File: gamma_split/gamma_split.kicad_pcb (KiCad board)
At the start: 2 copper layers, 109 x 71 mm, 156 parts, among them J1 USB_C_Receptacle, J2 USB_C_Receptacle, J3 TC2030-IDC, J4 D4, J5 D5, J6 A6, J7 A7, J8 B0, K00 K00, K01 K01, K02 K02, K03 K03, K04 K04, K05 K05, K10 K10, K11 K11, K12 K12, K13 K13, K14 K14, K15 K15, K20 K20, K21 K21, K22 K22, K23 K23, K24 K24, K25 K25, K30 K30, K31 K31, K32 K32, K33 K33, K34 K34, K35 K35, SW1 Switch-6P-2S2T, SW2 SW_Push, U1 MCP73831, U2 MCP1700 (3.0V), U3 MCP1700 (3.3V), U4 ATXMEGA-A4U-EPAD, U5 74LVC1G34, U6 nRF24L01_module, U7 FSUSB42, U8 FSUSB42, U9 FSUSB42

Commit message: rename alpha split to gamma split
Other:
- board text added: "γ-split"
- board text removed: "α-split"
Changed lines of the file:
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@@
       (net 10 /RST))
   )
-  (gr_text α-split (at 26 35.5) (layer F.SilkS)
+  (gr_text γ-split (at 26.5 35.5) (layer F.SilkS)
     (effects (font (size 1.5 1.5) (thickness 0.3)))
   )

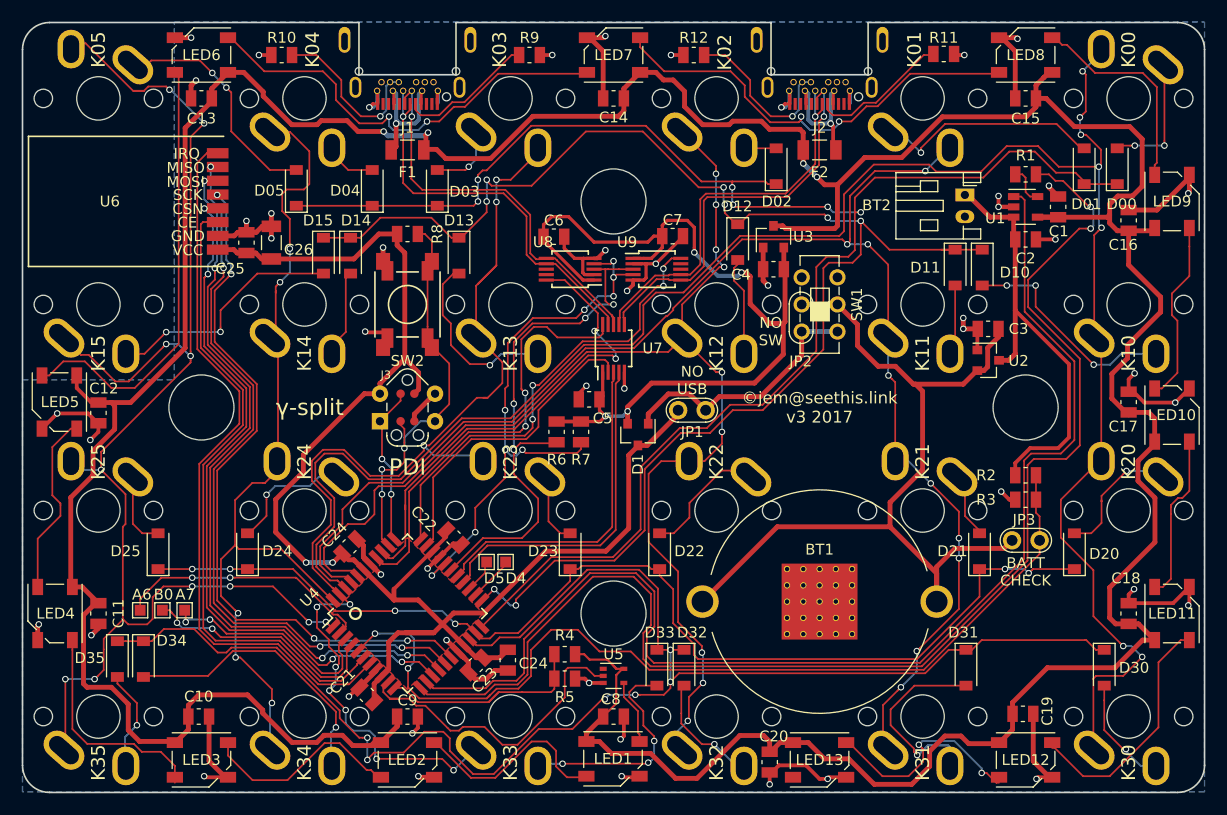
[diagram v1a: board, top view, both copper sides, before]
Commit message: remove soldermask around cr2032 battery contact
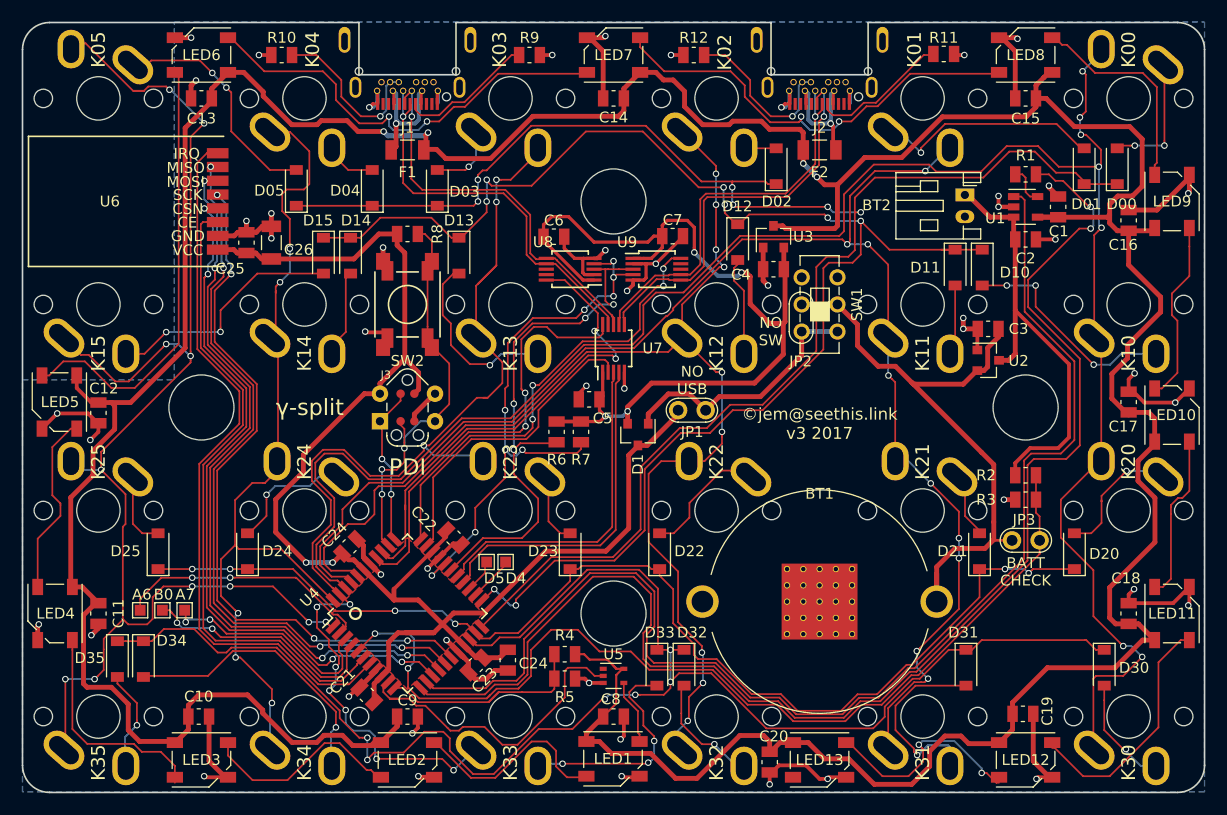
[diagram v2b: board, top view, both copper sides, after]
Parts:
- BT1: footprint battery:CR2032_BK-913 -> battery:CR2032_MPD_BK-913_NoSolderMask
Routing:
- net /BATT_IN: track 83.2 -> 59.9 mm
- net /ROW3: track 140.4 -> 145.2 mm
- net /ROW2: track 102.2 -> 106.2 mm
- net /BAT_LVL: track 87.7 -> 91.6 mm
- net /BAT_PROG: track 122.4 -> 126.3 mm
- net /BAT_STAT: track 113.1 -> 117.0 mm
- net /COL1: track 139.3 -> 141.3 mm
- net GND: track 184.7 -> 184.2 mm

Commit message: add some alternative xmegas
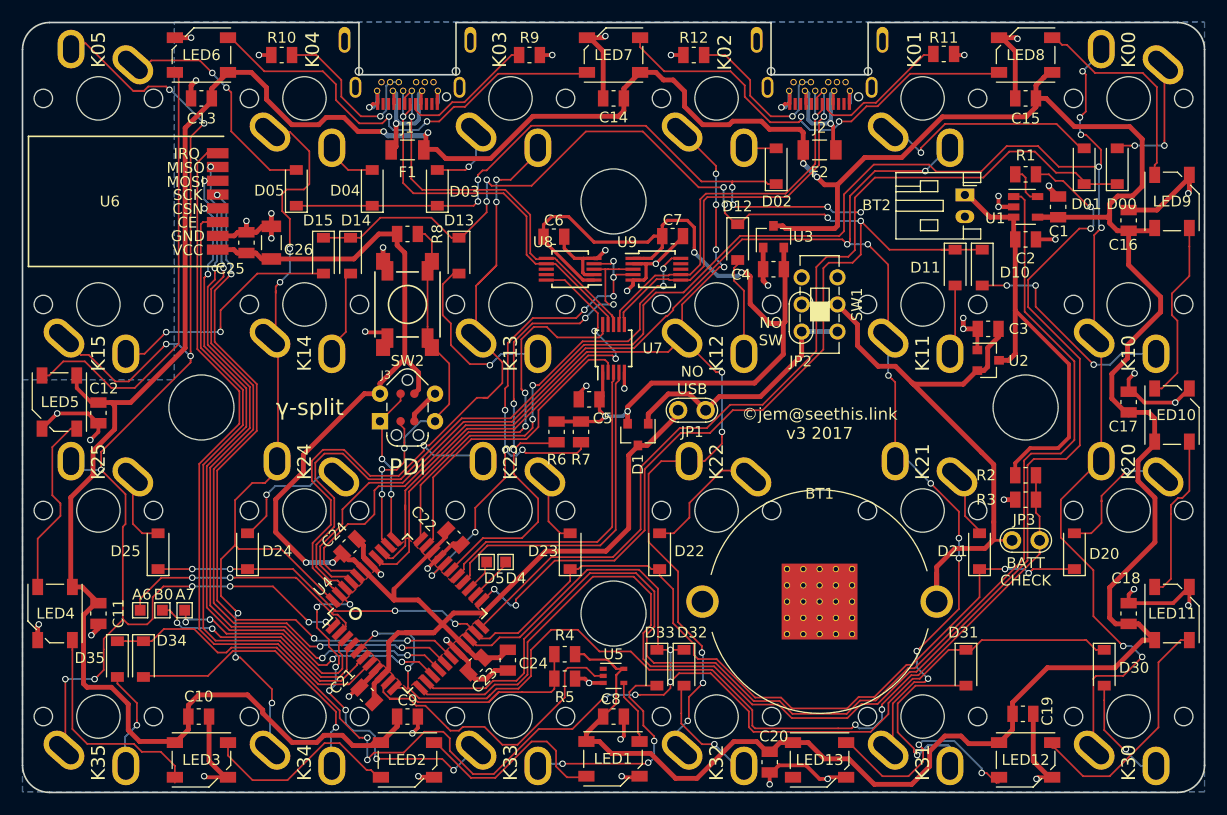
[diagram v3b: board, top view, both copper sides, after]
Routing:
- net /BAT_LVL: track 91.6 -> 94.1 mm, vias 2 -> 4
- net /ROW3: track 145.2 -> 146.4 mm
- net +5V: track 385.9 -> 385.3 mm
